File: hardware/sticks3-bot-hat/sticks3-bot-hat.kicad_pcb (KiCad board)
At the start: 2 copper layers, 48 x 33 mm, 23 parts, among them J1 HAT2_StickS3, J10 COLOR_B, J11 DC_6V_5525, J2 SERVO_A, J3 SERVO_B, J4 HEAD_PAN, J5 HEAD_TILT, J6 ENC_A, J7 ENC_B, J8 COLOR_A, U1 AP63205

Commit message: Bot HAT: dim power LED (R3 22k), M3 mounting holes, dockerised fab export
- R3 1k -> 22k (~0.14 mA): the 1k LED on the first JLCPCB batch was far
  too bright for a power indicator. BOM/LCSC updated (C4190).
- Mounting holes H1-H4 changed in place from MountingHole_2.7mm_M2.5 to
  MountingHole_3.2mm_M3, same centres; GND zones refilled. The M3 head
  courtyard grazes J1/J2 by <0.25 mm (DRC warning) - use <=5.5 mm heads.
- export.sh: falls back to the kicad/kicad:10.0 docker image when
  kicad-cli isn't installed, runs DRC/ERC, exports the schematic PDF,
  and no longer deletes the hand-maintained cpl-jlcpcb-corrected.csv.
- Regenerated gerbers, drill, positions, BOM, schematic PDF, reports.
- .gitignore .venv/
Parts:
- H1, H2, H3, H4: footprint MountingHole_2.7mm_M2.5 -> MountingHole:MountingHole_3.2mm_M3
- R3: value 1k -> 22k

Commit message: Bot HAT v4: LM393-order sensor headers, HC-SR04 DIST port, distance_sensor SDK
Board (hardware/sticks3-bot-hat, edited in place via gen/tools/rework_v4.py
so the hand routing survives):
- ENC A/B headers reordered to V G D0 and COLOR to V G - A0 (1x4) so the
  LM393 encoder / TCRT5000 modules connect with a straight Dupont cable.
- COLOR B replaced by DIST: 1x4 (5V TRIG ECHO GND) matching the HC-SR04,
  fed from the buck's 5 V; ECHO through a new 1k/2k divider (R4/R5) so the
  5 V pulse reaches G8 at 3.3 V; TRIG on the previously free G2.
- Power LED moved beside DIST. Schematic regenerated from design.py.
- DRC/ERC clean except the two known M3 courtyard warnings. Regenerated
  gerbers, drill, positions, BOM, JLC-corrected CPL (R3/D1/J10 moved,
  R4/R5 added), schematic PDF and renders (new gen/render.sh).
- gen_sch.py / export.sh / render.sh work with the kicad docker image.

Software:
- examples/sdk_distance_sensor.py: SPIKE-style distance(port) in mm
  (-1 out of range) plus distance_cm(); sdk_config gains
  DISTANCE_SENSOR_PINS, StickS3 color sensor is now port C on G1.
- Simulator: gears/minibot/distance_sensor.py on a forward UltrasonicSensor
  (in3, port D) added to robots/minibot.json; registered in skulpt.js.
- Scratch: "distance sensor (cm)" block; example.js lists the new SDK file.
- Docs: HAT README (connectors, GPIO map, ordering notes), CLAUDE.md,
  gears/README.md.
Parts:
- added R4: 1k, Resistor_SMD:R_0603_1608Metric, F.Cu at (91.5, 74.4)
- added R5: 2k, Resistor_SMD:R_0603_1608Metric, F.Cu at (93.9, 74.4)
- J10: value COLOR_B -> DIST; footprint PinHeader_1x03_P2.54mm_Vertical -> Connector_PinHeader_2.54mm:PinHeader_1x04_P2.54mm_Vertical
- J8: value COLOR_A -> COLOR; footprint PinHeader_1x03_P2.54mm_Vertical -> Connector_PinHeader_2.54mm:PinHeader_1x04_P2.54mm_Vertical
- moved D1 3.90 mm to (96.6, 74.4)
- moved R3 3.90 mm to (96.6, 71.3), turned to -90 degrees
- moved J10 2.54 mm to (86.2, 71.0)
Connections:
- J1 pad 14: (no net) -> TRIG
- J1 pad 7: COLOR_A -> COLOR
- J1 pad 9: COLOR_B -> ECHO
- J10 pad 1: COLOR_B -> +5V
- J10 pad 2: +3V3 -> TRIG
- J10 pad 3: GND -> ECHO_5V
- J6 pad 1: ENC_A -> +3V3
- J6 pad 2: +3V3 -> GND
- J6 pad 3: GND -> ENC_A
- J7 pad 1: ENC_B -> +3V3
- J7 pad 2: +3V3 -> GND
- J7 pad 3: GND -> ENC_B
- J8 pad 1: COLOR_A -> +3V3
- J8 pad 2: +3V3 -> GND
- J8 pad 3: GND -> (no net)
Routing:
- net GND: track 113.0 -> 17.8 mm, vias 3 -> 4
- net ECHO: track 0.00 -> 47.4 mm, vias 0 -> 2
- net TRIG: track 0.00 -> 35.6 mm, vias 0 -> 1
- net COLOR_B: track 33.2 -> 0.00 mm, vias 1 -> 0
- net COLOR: track 0.00 -> 29.0 mm, vias 0 -> 2
- net +3V3: track 64.5 -> 36.6 mm
- net COLOR_A: track 20.1 -> 0.00 mm, vias 1 -> 0
- net VSERVO: track 110.9 -> 102.6 mm, vias 2 -> 1
- net +5V: track 56.6 -> 64.7 mm
- net ENC_A: track 25.3 -> 29.8 mm, vias 1 -> 2
- net ECHO_5V: track 0.00 -> 2.65 mm
- net LED_K: track 3.82 -> 1.49 mm
- net ENC_B: track 19.7 -> 21.8 mm
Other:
- board text added: "-"
- board text added: "5"
- board text added: "A"
- board text added: "COLOR"
- board text added: "D"
- board text added: "DIST"
- board text added: "E"
- board text added: "G"
- board text added: "PySTEM Mini Bot - StickS3 HAT v4"
- board text added: "T"
- board text added: "V"
- board text removed: "COLOR A"
- board text removed: "COLOR B"
- board text removed: "PySTEM Mini Bot - StickS3 HAT v3"
- board text removed: "S 3V G"

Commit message: Bot HAT: drop the version from the silkscreen title; render with 3D models
The renders now use the kicad/kicad:10.0-full image (ships the KiCad 3D
model library) so headers, passives, the cap and the jack show as before.
Silkscreen/gerbers regenerated for the title change.
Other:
- board text added: "PySTEM Mini Bot - StickS3 HAT"
- board text removed: "PySTEM Mini Bot - StickS3 HAT v4"

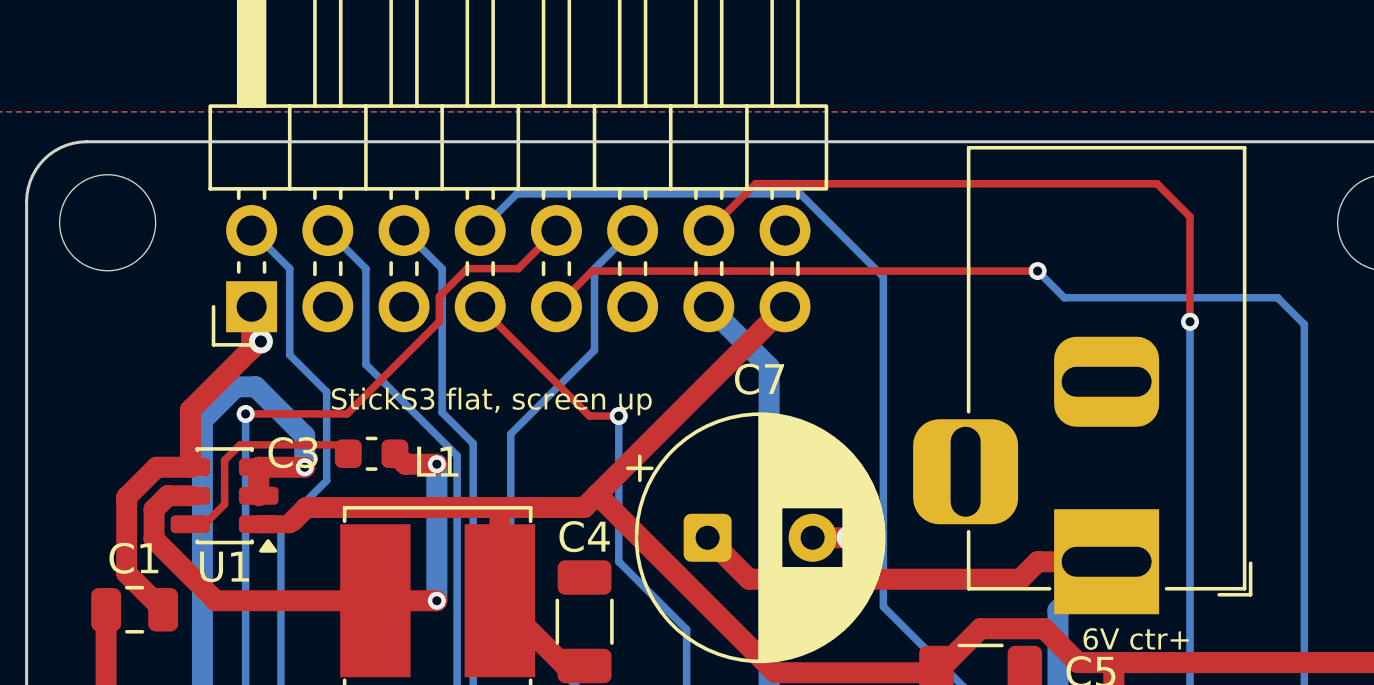
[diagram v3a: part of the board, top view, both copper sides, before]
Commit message: Bot HAT v5: swap the J1 header rows (StickS3 power row is the lower pins)
Bring-up of the v3 board showed the StickS3, screen up, puts its power row
(GND EXT_5V BOOT G1 G8 BAT 3V3 5V_IN) on the header's lower pins and the
GPIO row on the upper pins; design.py had them the other way round (copied
from M5Stack's table, whose numbering starts on the power row). Columns
were right. Every other part of the board checked out on hardware with an
11-wire Dupont harness swapping the rows: buck 5 V, servo rail, all four
servo headers, both encoders and the reflection sensor.

- design.py: J1 nets moved to the other row in each column; comment records
  the measured socket layout.
- kicad_pcb: gen/tools/rework_v5_j1rows.py (text edit, no pcbnew) drops the
  30 segments / 3 vias fanning out to J1, adds the re-terminated routes
  (35 segments / 3 vias), renets J1 and strips the stale zone fills.
  Nothing else on the board moved. Same-layer clearance checked >= 0.2 mm.
- kicad_sch: J1 pin labels / no-connects moved to match.
- README: header-row explanation, field fix for v3/v4 boards, corrected
  first-article checks, and the KiCad steps still to run on the Mac
  (refill zones, DRC, export.sh, render.sh).
- export.sh refills zones before export (KiCad bundle python or docker);
  stale v4 gerbers removed from fab/ so they cannot be ordered.
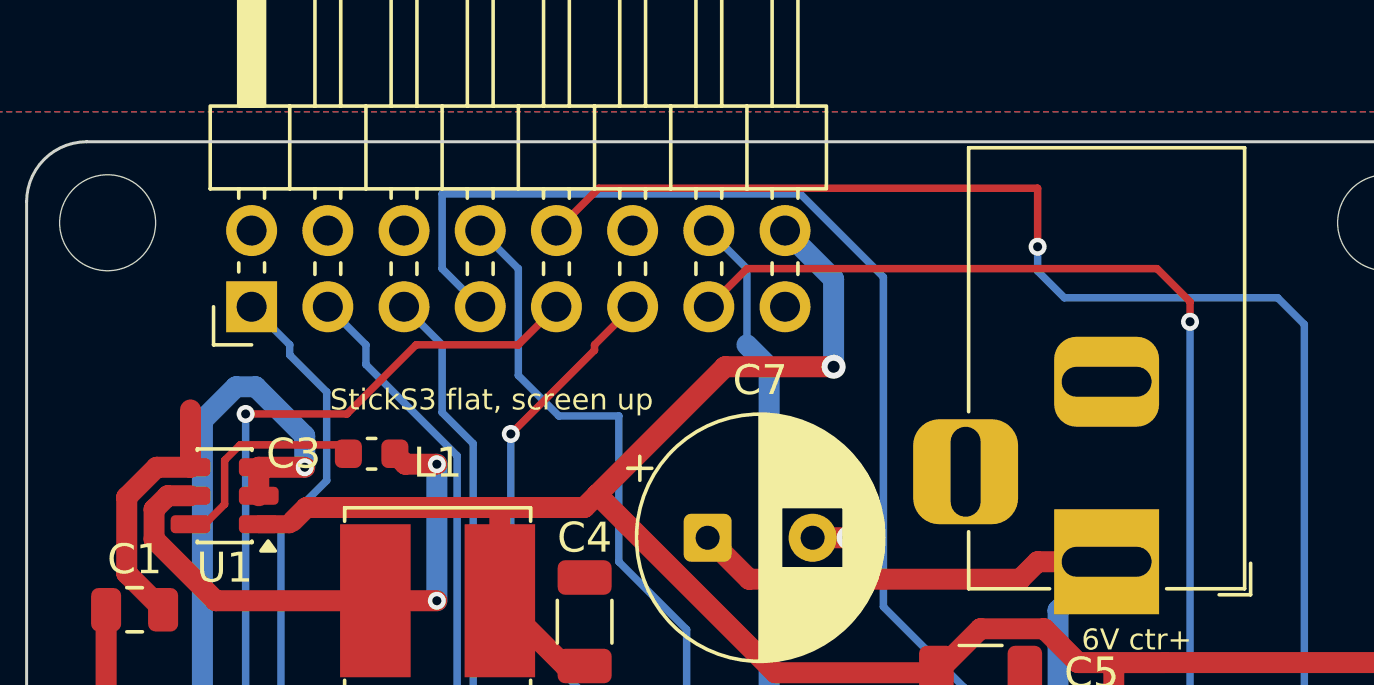
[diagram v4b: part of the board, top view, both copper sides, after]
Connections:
- J1 pad 1: GND -> SERVO_A
- J1 pad 10: ENC_A -> ECHO
- J1 pad 11: (no net) -> ENC_B
- J1 pad 12: ENC_B -> (no net)
- J1 pad 13: +3V3 -> TRIG
- J1 pad 14: TRIG -> +3V3
- J1 pad 15: +5V -> (no net)
- J1 pad 16: (no net) -> +5V
- J1 pad 2: SERVO_A -> GND
- J1 pad 3: (no net) -> SERVO_B
- J1 pad 4: SERVO_B -> (no net)
- J1 pad 5: (no net) -> PAN
- J1 pad 6: PAN -> (no net)
- J1 pad 7: COLOR -> TILT
- J1 pad 8: TILT -> COLOR
- J1 pad 9: ECHO -> ENC_A
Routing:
- net +5V: track 64.7 -> 70.7 mm, vias 0 -> 1
- net GND: track 17.8 -> 12.3 mm, vias 4 -> 3
- net TILT: track 38.9 -> 44.0 mm
- net COLOR: track 29.0 -> 32.1 mm, vias 2 -> 1
- net TRIG: track 35.6 -> 32.7 mm
- net ECHO: track 47.4 -> 50.2 mm
- net ENC_B: track 21.8 -> 19.3 mm, vias 0 -> 1
- net PAN: track 33.3 -> 30.7 mm
- net SERVO_B: track 25.8 -> 23.2 mm
- net SERVO_A: track 25.4 -> 22.9 mm
- net +3V3: track 36.6 -> 39.2 mm
- net ENC_A: track 29.8 -> 28.2 mm
